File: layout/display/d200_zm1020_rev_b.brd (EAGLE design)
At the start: 200 x 50 mm, 81 parts, among them IC1 STM32F103C8T, IC2 LP2985-SOT23-5, IC3 IC_USBLC6-2, IC4 IC_USBLC6-2, IC5 LT1619ES8, IC6 LP2985-SOT23-5, IC7 IRF7470, SW1 2P2T, T1 LPISR, Y1 532-CRYSTAL, Y2 EQ161-CRYSTAL

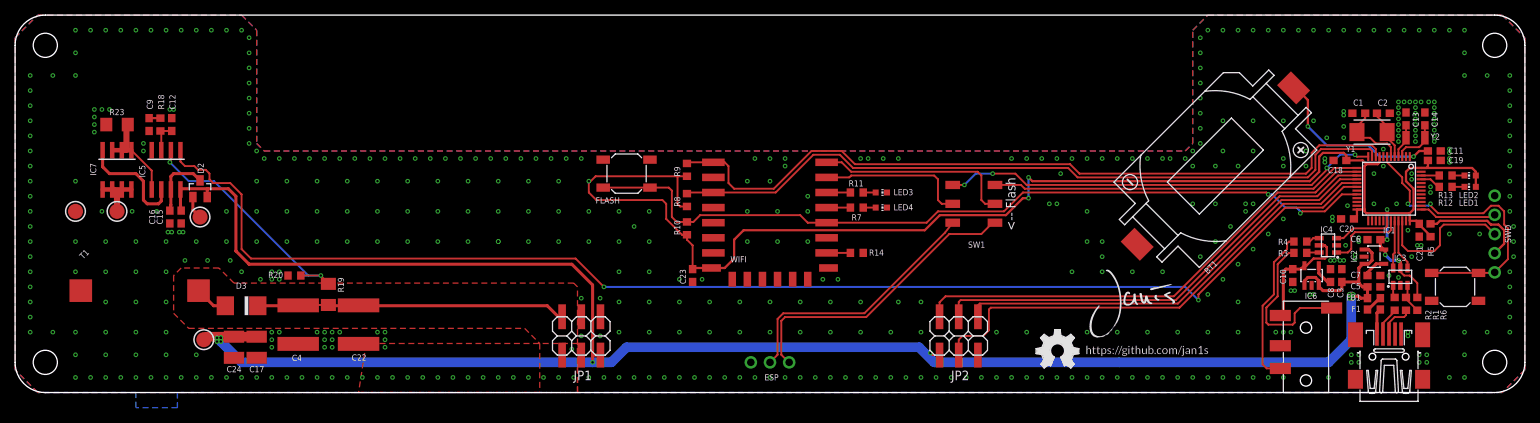
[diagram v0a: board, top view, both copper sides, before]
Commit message: Added rev. B of large clock layouts
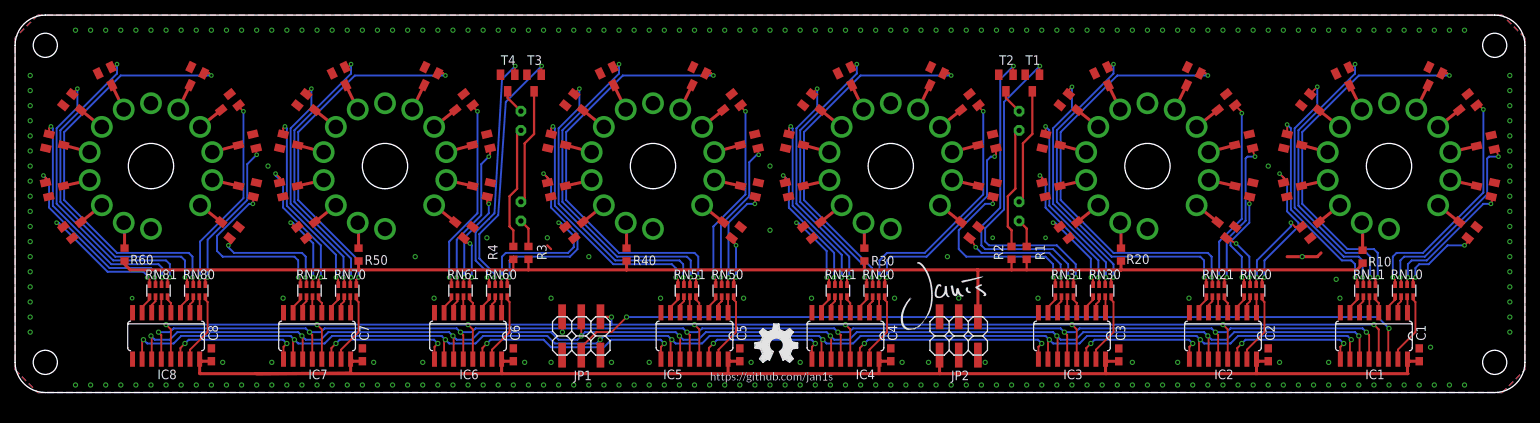
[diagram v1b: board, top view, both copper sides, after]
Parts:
- removed BT1: CR2032-HOLDER, battery-holder:CH28-2032LF
- removed C10, C11: 10µF/6.3V, rcl:C0603
- removed C12: 22nF, rcl:C0603
- removed C13, C14: 10p, rcl:C0603
- removed C15, C16: 10µF, rcl:C0603
- removed C17, C24: 100µF/6.3V, rcl:C1210
- removed C18, C23: 1µF, rcl:C0603
- removed C19, C20, C21: 100nF, rcl:C0603
- removed C22: 1µF/250V, rcl:C2220K
- removed C9: 150pF, rcl:C0603
- removed D2: BAT54C, diode:SOT23
- removed D3: ES2, diode:DO-214AA
- removed ESP: (no value), microbuilder:1X03_ROUND
- removed F1, R12, R13: 1k, rcl:R0603
- removed FB1: EMI, rcl:R0603
- removed FLASH, ISP: TACT-SWITCH-40-40, tactile-switch:40-40
- removed LED1, LED2, LED3, LED4: (no value), led:CHIP-LED0603
- removed LOGO1, LOGO2: OSHW_LOGO_FILLX0200-NT, ohw-logo:OSHW_FILLX200_NOTEXT
- removed R11, R14, R7, R8, R9: 10k, rcl:R0603
- removed R18: 82k, rcl:R0603
- removed R19: 1M, rcl:M1206
- removed R23: 0.01R, rcl:R1206
- removed R5: 33R, rcl:R0603
- removed R6: 1k5, rcl:R0603
- removed SW1: 2P2T, switch:MSS22D18
- removed SWD: (no value), microbuilder:1X05_ROUND
- removed TP1, TP2, TP3, TP4: (no value), microbuilder:TESTPOINT_ROUND_2MM
- removed TRS1: PJ-3504, con-trs:YD-PJ-3504
- removed WIFI: ESP-12F, espressif:ESP-12F
- removed X1: (no value), con-cypressindustries:32005-201
- removed Y1: 532-CRYSTAL, euroquartz:2PIN50X32
- removed Y2: EQ161-CRYSTAL, euroquartz:EQ161
- added GL1, GL2, GL3, GL4: (no value), nixie_tube:NE2-NEON-BULB-DRILL
- added IC8: 74HC595D, 74xx-eu:SO16
- added R30, R40, R50, R60: (no value), rcl:R0603
- added RN10, RN11, RN20, RN21, RN30, RN31, RN40, RN41, RN50, RN51, RN60, RN61, RN70, RN71, RN80, RN81: (no value), resistor-net:CTS742C083
- added T10, T11, T12, T13, T14, T15, T16, T17, T18, T19, T2, T20, T21, T22, T23, T24, T25, T26, T27, T28, T29, T3, T30, T31, T32, T33, T34, T35, T36, T37, T38, T39, T4, T40, T41, T42, T43, T44, T45, T46, T47, T48, T49, T50, T51, T52, T53, T54, T55, T56, T57, T58, T59, T60, T61, T62, T63, T64, T65, T66, T67, T68, T69: (no value), transistor-hv:SOT23
- added U$3: (no value), pcb-artwork:GITHUB/JAN1S
- added U$4, U$7, U$8, U$9: ZM1020, nixietubes-western:ZM1020
- C1, C2: value 10p -> (none)
- C3, C5, C6: value 10µF/6.3V -> (none)
- C4: value 1µF/250V -> (none); device rcl:C2220K -> rcl:C0603
- C7, C8: value 10nF -> (none)
- IC1: value STM32F103C8T -> 74HC595D; device micro-stm_v3:LQFP48 -> 74xx-eu:SO16
- IC2, IC6: value LP2985-SOT23-5 -> 74HC595D; device vreg:SOT23-5 -> 74xx-eu:SO16
- IC3, IC4: value IC_USBLC6-2 -> 74HC595D; device dp_devices:SOT-23-6L -> 74xx-eu:SO16
- IC5: value LT1619ES8 -> 74HC595D; device lt:SO8 -> 74xx-eu:SO16
- IC7: value IRF7470 -> 74HC595D; device ir:SO8 -> 74xx-eu:SO16
- R1, R2, R3, R4: value 33R -> (none)
- R10: value 10k -> (none)
- R20: value 8k2 -> (none)
- T1: value LPISR -> (none); device fastron:PISR -> transistor-hv:SOT23
- U$1: device pcb-artwork:JANIS_10MM -> ohw-logo:OSHW_FILLX200_NOTEXT
- U$5, U$6: value (none) -> ZM1020; device pcb-artwork:GITHUB/JAN1S -> nixietubes-western:ZM1020
- moved C8 148.6 mm to (26.0, 5.00)
- moved C7 134.4 mm to (46.0, 5.00), turned to 90 degrees
- moved T1 121.4 mm to (134.8, 41.0), turned to 180 degrees
- moved C6 115.0 mm to (66.0, 5.00), turned to 90 degrees
- moved IC6 112.0 mm to (60.0, 7.50), turned to 180 degrees
- moved R20 109.5 mm to (146.5, 18.3), turned to 270 degrees
- moved R4 104.3 mm to (66.0, 18.5), turned to 270 degrees
- moved R3 102.2 mm to (68.0, 18.5), turned to 270 degrees
- moved R10 89.6 mm to (178.5, 18.0)
- moved C5 84.5 mm to (96.0, 5.00), turned to 90 degrees
- moved C4 78.6 mm to (116.0, 5.00), turned to 90 degrees
- moved IC5 73.4 mm to (90.0, 7.50)
- moved IC4 63.9 mm to (110.0, 7.50), turned to 180 degrees
- moved R2 51.2 mm to (132.0, 18.5), turned to 270 degrees
- moved R1 50.7 mm to (134.0, 18.5), turned to 270 degrees
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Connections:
- removed net +3V3: C18.1, C19.1, C20.1, C21.1, C23.1, C6.1, IC1.24, IC1.36, IC1.48, IC1.9, IC2.5, IC3.5, LED1.A, LED2.A, R10.2, R5.2, R6.1, R8.2, R9.2, WIFI.8
- removed net ASDAWJIODJA: R5.1, SWD.4
- removed net HV: C22.1, C4.1, D3.C, JP1.2, R19.2
- removed net HV_EN: IC1.18, IC5.1
- removed net I2C1_SCL: IC1.42
- removed net I2C1_SDA: IC1.43
- removed net I2C2_SCL: IC1.21
- removed net I2C2_SDA: IC1.22
- removed net JNTRST: IC1.40
- removed net JTDI: IC1.38
- removed net JTDO: IC1.39
- removed net LED_BOOT: IC1.46, R13.1
- removed net LED_FIX: IC1.45, R12.1
- removed net N$22: F1.2, FB1.2
- removed net N$23: IC3.1, R2.2
- removed net N$24: R2.1, X1.2
- removed net N$25: IC4.4, R4.2
- removed net N$26: SW1.C2, WIFI.21
- removed net N$27: R11.1, WIFI.20
- removed net N$28: R3.1, TRS1.5
- removed net N$29: C13.1, IC1.4, Y2.P$1
- removed net N$30: C14.1, IC1.3, Y2.P$2
- removed net N$31: ESP.3, SW1.B1
- removed net N$32: ESP.2, SW1.B2
- removed net N$33: R7.1, WIFI.19
- removed net N$34: LED4.A, R7.2
- removed net N$35: LED3.A, R11.2
- removed net N$36: R1.1, X1.3
- removed net N$38: IC1.29
- removed net N$48: IC1.41
- removed net N$55: IC1.25
- removed net NX_EN: IC1.14, JP2.2
- removed net NX_RCK: IC1.16, JP2.6
- removed net RESET: IC1.7, ISP.3, ISP.4, SWD.5
- removed net RFMOD_DBG: IC1.19
- removed net RFMOD_EN: IC1.11, R8.1, WIFI.3
- removed net RFMOD_FLASH: FLASH.3, FLASH.4, IC1.20, R10.1, WIFI.18
- removed net RFMOD_RST: IC1.10, R9.1, WIFI.1
- removed net RTC-TAMPER: IC1.2
- removed net SPI1_MOSI: IC1.17, JP2.3
- removed net SPI1_SCK: IC1.15, JP2.4
- removed net SPI2_MISO: IC1.27
- removed net SPI2_MOSI: IC1.28
- removed net SPI2_SCK: IC1.26
- removed net SWCLK: IC1.37, SWD.2
- removed net SWDIO: IC1.34, SWD.3
- removed net TRS_VCC: C10.1, IC4.5, IC6.5, TRS1.4
- removed net USART1_RX: IC1.31, IC4.1
- removed net USART1_TX: IC1.30, IC4.3
- removed net USART2_RX: IC1.13, SW1.A1
- removed net USART2_TX: IC1.12, SW1.A2
- removed net USB_DM: IC1.32, IC3.6
- removed net USB_DP: IC1.33, IC3.4
- removed net VBAT: BT1.POS, C11.1, IC1.1
- new net 1A: IC1.15, RN10.4
- new net 1B: IC1.1, RN10.3
- new net 1C: IC1.2, RN10.2
- new net 1D: IC1.3, RN10.1
- new net 1E: IC1.4, RN11.4
- new net 1F: IC1.5, RN11.3
- new net 1G: IC1.6, RN11.2
- new net 1H: IC1.7, RN11.1
- new net 2A: IC2.15, RN20.4
- new net 2B: IC2.1, RN20.3
- new net 2C: IC2.2, RN20.2
- new net 2D: IC2.3, RN20.1
- new net 2E: IC2.4, RN21.4
- new net 2F: IC2.5, RN21.3
- new net 2G: IC2.6, RN21.2
- new net 2H: IC2.7, RN21.1
- new net 3A: IC3.15, RN30.4
- new net 3B: IC3.1, RN30.3
- new net 3C: IC3.2, RN30.2
- new net 3D: IC3.3, RN30.1
- new net 3E: IC3.4, RN31.4
- new net 3F: IC3.5, RN31.3
- new net 3G: IC3.6, RN31.2
- new net 3H: IC3.7, RN31.1
- new net 4A: IC4.15, RN40.4
- new net 4B: IC4.1, RN40.3
- new net 4C: IC4.2, RN40.2
- new net 4D: IC4.3, RN40.1
- new net 4E: IC4.4, RN41.4
- new net 4F: IC4.5, RN41.3
- new net 4G: IC4.6, RN41.2
- new net 4H: IC4.7, RN41.1
- new net 5A: IC5.15, RN50.4
- new net 5B: IC5.1, RN50.3
- new net 5C: IC5.2, RN50.2
- new net 5D: IC5.3, RN50.1
- new net 5E: IC5.4, RN51.4
- new net 5F: IC5.5, RN51.3
- new net 5G: IC5.6, RN51.2
- new net 5H: IC5.7, RN51.1
- new net 6A: IC6.15, RN60.4
- new net 6B: IC6.1, RN60.3
- new net 6C: IC6.2, RN60.2
- new net 6D: IC6.3, RN60.1
- new net 6E: IC6.4, RN61.4
- new net 6F: IC6.5, RN61.3
- new net 6G: IC6.6, RN61.2
- new net 6H: IC6.7, RN61.1
- new net 7A: IC7.15, RN70.4
- new net 7B: IC7.1, RN70.3
- new net 7C: IC7.2, RN70.2
- new net 7D: IC7.3, RN70.1
- new net 7E: IC7.4, RN71.4
- new net 7F: IC7.5, RN71.3
- new net 7G: IC7.6, RN71.2
- new net 7H: IC7.7, RN71.1
- new net 8A: IC8.15, RN80.4
- new net 8B: IC8.1, RN80.3
- new net 8C: IC8.2, RN80.2
- new net 8D: IC8.3, RN80.1
- new net 8E: IC8.4, RN81.4
- new net 8F: IC8.5, RN81.3
- new net 8G: IC8.6, RN81.2
- new net 8H: IC8.7, RN81.1
- new net EN: IC1.13, IC2.13, IC3.13, IC4.13, IC5.13, IC6.13, IC7.13, IC8.13, JP1.1
- new net GL1: RN31.5, T1.1
- new net GL2: RN31.6, T2.1
- new net GL3: RN60.7, T3.1
- new net GL4: RN60.8, T4.1
- new net MOSI: IC1.14, JP1.4
- new net N1_B0: RN20.6, T11.1
- new net N1_B1: RN10.5, T12.1
- new net N1_B2: RN10.6, T13.1
- new net N1_B3: RN10.7, T16.1
- new net N1_B4: RN10.8, T14.1
- new net N1_B5: RN11.5, T15.1
- new net N1_B6: RN11.6, T17.1
- new net N1_B7: RN11.7, T18.1
- new net N1_B8: RN11.8, T19.1
- new net N1_B9: RN20.5, T10.1
- new net N1_K0: T11.3, U$4.P3
- new net N1_K1: T12.3, U$4.P13
- new net N1_K2: T13.3, U$4.P12
- new net N1_K3: T16.3, U$4.P11
- new net N1_K4: T14.3, U$4.P10
- new net N1_K5: T15.3, U$4.P9
- new net N1_K6: T17.3, U$4.P7
- new net N1_K7: T18.3, U$4.P6
- new net N1_K8: T19.3, U$4.P5
- new net N1_K9: T10.3, U$4.P4
- new net N2_B0: RN30.8, T21.1
- new net N2_B1: RN20.7, T22.1
- new net N2_B2: RN20.8, T23.1
- new net N2_B3: RN21.5, T26.1
- new net N2_B4: RN21.6, T24.1
- new net N2_B5: RN21.7, T25.1
- new net N2_B6: RN21.8, T27.1
- new net N2_B7: RN30.5, T28.1
- new net N2_B8: RN30.6, T29.1
- new net N2_B9: RN30.7, T20.1
- new net N2_K0: T21.3, U$5.P3
- new net N2_K1: T22.3, U$5.P13
- new net N2_K2: T23.3, U$5.P12
- new net N2_K3: T26.3, U$5.P11
- new net N2_K4: T24.3, U$5.P10
- new net N2_K5: T25.3, U$5.P9
- new net N2_K6: T27.3, U$5.P7
- new net N2_K7: T28.3, U$5.P6
- new net N2_K8: T29.3, U$5.P5
- new net N2_K9: T20.3, U$5.P4
- new net N3_B0: RN41.8, T31.1
- new net N3_B1: RN31.7, T32.1
- new net N3_B2: RN31.8, T33.1
- new net N3_B3: RN40.5, T36.1
- new net N3_B4: RN40.6, T34.1
- new net N3_B5: RN40.7, T35.1
- new net N3_B6: RN40.8, T37.1
- new net N3_B7: RN41.5, T38.1
- new net N3_B8: RN41.6, T39.1
- new net N3_B9: RN41.7, T30.1
- new net N3_K0: T31.3, U$6.P3
- new net N3_K1: T32.3, U$6.P13
- new net N3_K2: T33.3, U$6.P12
- new net N3_K3: T36.3, U$6.P11
- new net N3_K4: T34.3, U$6.P10
- new net N3_K5: T35.3, U$6.P9
- new net N3_K6: T37.3, U$6.P7
- new net N3_K7: T38.3, U$6.P6
- new net N3_K8: T39.3, U$6.P5
- new net N3_K9: T30.3, U$6.P4
- new net N4_B0: RN60.6, T41.1
- new net N4_B1: RN50.5, T42.1
- new net N4_B2: RN50.6, T43.1
- new net N4_B3: RN50.7, T46.1
- new net N4_B4: RN50.8, T44.1
- new net N4_B5: RN51.5, T45.1
- new net N4_B6: RN51.6, T47.1
- new net N4_B7: RN51.7, T48.1
- new net N4_B8: RN51.8, T49.1
- new net N4_B9: RN60.5, T40.1
- new net N4_K0: T41.3, U$7.P3
- new net N4_K1: T42.3, U$7.P13
- new net N4_K2: T43.3, U$7.P12
- new net N4_K3: T46.3, U$7.P11
- new net N4_K4: T44.3, U$7.P10
- new net N4_K5: T45.3, U$7.P9
- new net N4_K6: T47.3, U$7.P7
- new net N4_K7: T48.3, U$7.P6
- new net N4_K8: T49.3, U$7.P5
- new net N4_K9: T40.3, U$7.P4
- new net N5_B0: RN71.6, T51.1
- new net N5_B1: RN61.5, T52.1
- new net N5_B2: RN61.6, T53.1
- new net N5_B3: RN61.7, T56.1
- new net N5_B4: RN61.8, T54.1
- new net N5_B5: RN70.5, T55.1
- new net N5_B6: RN70.6, T57.1
- new net N5_B7: RN70.7, T58.1
- new net N5_B8: RN70.8, T59.1
- new net N5_B9: RN71.5, T50.1
- new net N5_K0: T51.3, U$8.P3
- new net N5_K1: T52.3, U$8.P13
- new net N5_K2: T53.3, U$8.P12
- new net N5_K3: T56.3, U$8.P11
- new net N5_K4: T54.3, U$8.P10
- new net N5_K5: T55.3, U$8.P9
- new net N5_K6: T57.3, U$8.P7
- new net N5_K7: T58.3, U$8.P6
- new net N5_K8: T59.3, U$8.P5
- new net N5_K9: T50.3, U$8.P4
- new net N6_B0: RN81.8, T61.1
- new net N6_B1: RN71.7, T62.1
- new net N6_B2: RN71.8, T63.1
- new net N6_B3: RN80.5, T66.1
- new net N6_B4: RN80.6, T64.1
- new net N6_B5: RN80.7, T65.1
- new net N6_B6: RN80.8, T67.1
- new net N6_B7: RN81.5, T68.1
- new net N6_B8: RN81.6, T69.1
- new net N6_B9: RN81.7, T60.1
- new net N6_K0: T61.3, U$9.P3
- new net N6_K1: T62.3, U$9.P13
- new net N6_K2: T63.3, U$9.P12
- new net N6_K3: T66.3, U$9.P11
- new net N6_K4: T64.3, U$9.P10
- new net N6_K5: T65.3, U$9.P9
- new net N6_K6: T67.3, U$9.P7
- new net N6_K7: T68.3, U$9.P6
- new net N6_K8: T69.3, U$9.P5
- new net N6_K9: T60.3, U$9.P4
- new net RCK: IC1.12, IC2.12, IC3.12, IC4.12, IC5.12, IC6.12, IC7.12, IC8.12, JP1.5
- new net SCK: IC1.11, IC2.11, IC3.11, IC4.11, IC5.11, IC6.11, IC7.11, IC8.11, JP1.3
- new net SCL: IC1.10, IC2.10, IC3.10, IC4.10, IC5.10, IC6.10, IC7.10, IC8.10, JP1.2
- new net VDD: JP2.1, R1.2, R10.2, R2.2, R20.2, R3.2, R30.2, R4.2, R40.2, R50.2, R60.2
- net +5V: now also C1.1, C2.1, C4.1, C6.1, C7.1, C8.1, IC1.16, IC2.16, IC3.16, IC4.16, IC5.16, IC6.16, IC7.16, IC8.16, JP2.6; no longer C15.1, C17.1, C24.1, D2.2, FB1.1, IC2.1, IC2.3, IC5.8, IC6.1, IC6.3, JP1.5, JP2.1, TP1.P$1
- net GND: now also IC2.8, IC3.8, IC4.8, IC5.8, IC6.8, IC7.8, IC8.8, JP2.2, JP2.3, JP2.4, T1.2, T10.2, T11.2, T12.2, T13.2, T14.2, T15.2, T16.2, T17.2, T18.2, T19.2, T2.2, T20.2, T21.2, T22.2, T23.2, T24.2, T25.2, T26.2, T27.2, T28.2, T29.2, T3.2, T30.2, T31.2, T32.2, T33.2, T34.2, T35.2, T36.2, T37.2, T38.2, T39.2, T4.2, T40.2, T41.2, T42.2, T43.2, T44.2, T45.2, T46.2, T47.2, T48.2, T49.2, T50.2, T51.2, T52.2, T53.2, T54.2, T55.2, T56.2, T57.2, T58.2, T59.2, T60.2, T61.2, T62.2, T63.2, T64.2, T65.2, T66.2, T67.2, T68.2, T69.2; no longer BT1.NEG, C10.2, C11.2, C12.2, C13.2, C14.2, C15.2, C16.2, C17.2, C18.2, C19.2, C20.2, C21.2, C22.2, C23.2, C24.2, C9.2, ESP.1, FLASH.1, FLASH.2, IC1.23, IC1.35, IC1.44, IC1.47, IC2.2, IC3.2, IC4.2, IC5.4, IC6.2, ISP.1, ISP.2, JP1.1, JP1.3, JP1.4, LED3.C, LED4.C, R14.2, R20.2, R23.1, SWD.1, T1.P$2, TP4.P$1, TRS1.3, WIFI.15, X1.5, X1.M1, X1.M2, X1.M3, X1.M4
- net N$1: now also GL2.1, R2.1; no longer C1.1, IC1.6, Y1.P$1
- net N$10: now also IC1.9, IC2.14; no longer LED2.C, R13.2
- net N$11: now also IC2.9, IC3.14; no longer LED1.C, R12.2
- net N$12: now also IC3.9, IC4.14; no longer R4.1, TRS1.2
- net N$13: now also R30.1, U$6.P2; no longer IC7.5, IC7.6, IC7.7, IC7.8, TP2.P$1
- net N$14: now also R40.1, U$7.P2; no longer C12.1, IC5.3, R18.1
- net N$15: now also R50.1, U$8.P2; no longer C9.1, R18.2
- net N$16: now also IC4.9, IC5.14; no longer D3.A, T1.P$1
- net N$17: now also R60.1, U$9.P2; no longer IC5.2, R19.1, R20.1
- net N$18: now also IC5.9, IC6.14; no longer IC5.5, IC7.1, IC7.2, IC7.3, R23.2
- net N$19: now also IC6.9, IC7.14; no longer C16.1, D2.3, IC5.7
- net N$2: now also GL3.1, R3.1; no longer C2.1, IC1.5, Y1.P$2
- net N$20: now also IC7.9, IC8.14; no longer C7.1, IC2.4
- net N$21: now also GL1.1, R1.1; no longer SW1.C1, WIFI.22
- net N$3: now also GL4.1, R4.1; no longer F1.1, X1.1
- net N$4: now also R10.1, U$4.P2; no longer C8.1, IC6.4
- net N$5: now also GL2.2, T2.3; no longer IC3.3, R1.2, R6.2
- net N$6: now also GL1.2, T1.3; no longer R14.1, WIFI.16
- net N$7: now also GL4.2, T4.3; no longer IC4.6, R3.2
- net N$8: now also GL3.2, T3.3; no longer D2.1, TP3.P$1
- net N$9: now also R20.1, U$5.P2; no longer IC5.6, IC7.4
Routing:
- net EN: track 0.00 -> 202.6 mm, vias 0 -> 9
- net +3V3: track 199.5 -> 0.00 mm, vias 6 -> 0
- net RCK: track 0.00 -> 195.3 mm, vias 0 -> 9
- net SCK: track 0.00 -> 194.1 mm, vias 0 -> 9
- net SCL: track 0.00 -> 189.9 mm, vias 0 -> 9
- net VDD: track 0.00 -> 181.7 mm
- net HV_EN: track 176.3 -> 0.00 mm, vias 2 -> 0
- net MOSI: track 0.00 -> 114.4 mm, vias 0 -> 2
- net RFMOD_FLASH: track 108.5 -> 0.00 mm, vias 2 -> 0
- net RFMOD_RST: track 101.3 -> 0.00 mm
- net RFMOD_EN: track 97.7 -> 0.00 mm
- net +5V: track 298.4 -> 216.3 mm, vias 11 -> 0
- net SPI1_MOSI: track 65.0 -> 0.00 mm
- net NX_EN: track 64.4 -> 0.00 mm
- net SPI1_SCK: track 61.6 -> 0.00 mm
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- removed copper zone on layer 1, net +5V
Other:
- board text removed: "<-- Flash"
- board text removed: "GND"
- board text removed: "RST"
- board text removed: "RX"
- board text removed: "SWCLK"
- board text removed: "SWDIO"
- board text removed: "TX"
- board text removed: "VCC"
